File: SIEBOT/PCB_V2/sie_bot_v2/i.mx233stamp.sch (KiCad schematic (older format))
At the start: 0 parts

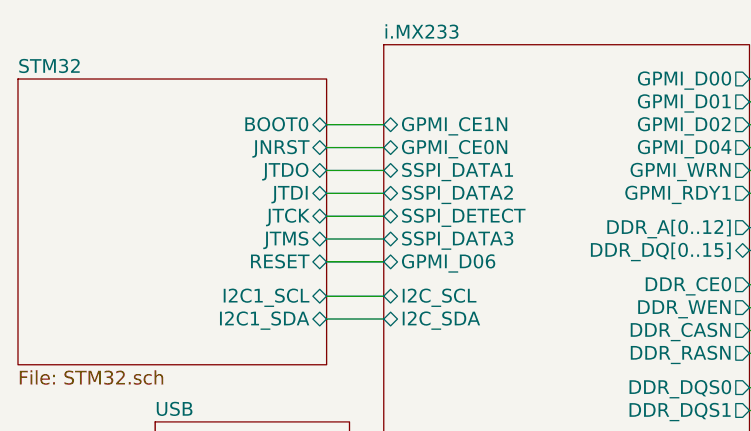
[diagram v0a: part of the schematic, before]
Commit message: Adición de ejemplos, modificación de los fuentes de elua para soportar el stm32f105
Cambios en el PCB para tener comunicación entre el IMX y el STM32 por puerto serial e i2c
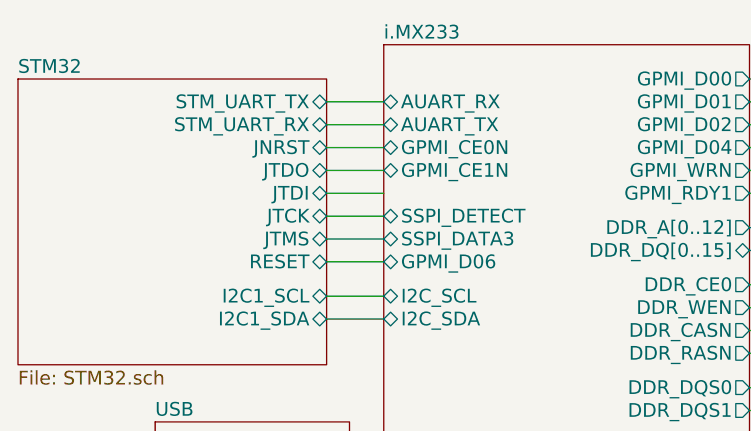
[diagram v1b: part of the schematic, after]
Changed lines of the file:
@@
-EESchema Schematic File Version 2  date Sat 21 Jan 2012 09:46:46 PM COT
+EESchema Schematic File Version 2  date Fri 10 Feb 2012 10:54:05 AM COT
 LIBS:con-jack
 LIBS:adm3101e
@@
 Sheet 1 5
 Title ""
-Date "22 jan 2012"
+Date "10 feb 2012"
 Rev ""
 Comp ""
@@
 $EndDescr
 Wire Wire Line
+	2900 1950 3150 1950
+Wire Wire Line
 	3150 2800 2900 2800
 Wire Wire Line
@@
 	3000 3950 3150 3950
 Wire Wire Line
-	2900 1950 3150 1950
-Wire Wire Line
 	2900 2150 3150 2150
 Wire Wire Line
@@
 Wire Wire Line
 	2900 2700 3150 2700
-$Sheet
-S 1550 1750 1350 1250
-U 4E78AF25
-F0 "STM32" 60
-F1 "STM32.sch" 60
-F2 "BOOT0" B R 2900 1950 60
-F3 "JNRST" B R 2900 2050 60
-F4 "JTMS" B R 2900 2450 60
-F5 "JTCK" B R 2900 2350 60
-F6 "JTDO" B R 2900 2150 60
-F7 "JTDI" B R 2900 2250 60
-F8 "RESET" B R 2900 2550 60
-F9 "I2C1_SCL" B R 2900 2700 60
-F10 "I2C1_SDA" B R 2900 2800 60
-$EndSheet
+Wire Wire Line
+	2900 1850 3150 1850
 $Sheet
 S 3150 1600 1600 2950
@@
 F30 "I2C_SDA" B L 3150 2800 60
 F31 "GPMI_CE0N" B L 3150 2050 60
-F32 "SSPI_DATA1" B L 3150 2150 60
-F33 "SSPI_DETECT" B L 3150 2350 60
-F34 "SSPI_DATA2" B L 3150 2250 60
-F35 "GPMI_CE1N" B L 3150 1950 60
-F36 "GPMI_D06" B L 3150 2550 60
-F37 "SSPI_DATA3" B L 3150 2450 60
-F38 "USM_P2" B L 3150 4150 60
-F39 "USB_M2" B L 3150 4250 60
+F32 "SSPI_DETECT" B L 3150 2350 60
+F33 "GPMI_CE1N" B L 3150 2150 60
+F34 "GPMI_D06" B L 3150 2550 60
+F35 "SSPI_DATA3" B L 3150 2450 60
+F36 "USM_P2" B L 3150 4150 60
+F37 "USB_M2" B L 3150 4250 60
+F38 "AUART_TX" B L 3150 1950 60
+F39 "AUART_RX" B L 3150 1850 60
 $EndSheet
 $Sheet
+S 1550 1750 1350 1250
+U 4E78AF25
+F0 "STM32" 60
+F1 "STM32.sch" 60
+F2 "JNRST" B R 2900 2050 60
+F3 "JTMS" B R 2900 2450 60
+F4 "JTCK" B R 2900 2350 60
+F5 "JTDO" B R 2900 2150 60
+F6 "JTDI" B R 2900 2250 60
+F7 "RESET" B R 2900 2550 60
+F8 "I2C1_SCL" B R 2900 2700 60
+F9 "I2C1_SDA" B R 2900 2800 60
+F10 "STM_UART_TX" B R 2900 1850 60
+F11 "STM_UART_RX" B R 2900 1950 60
+$EndSheet
+$Sheet

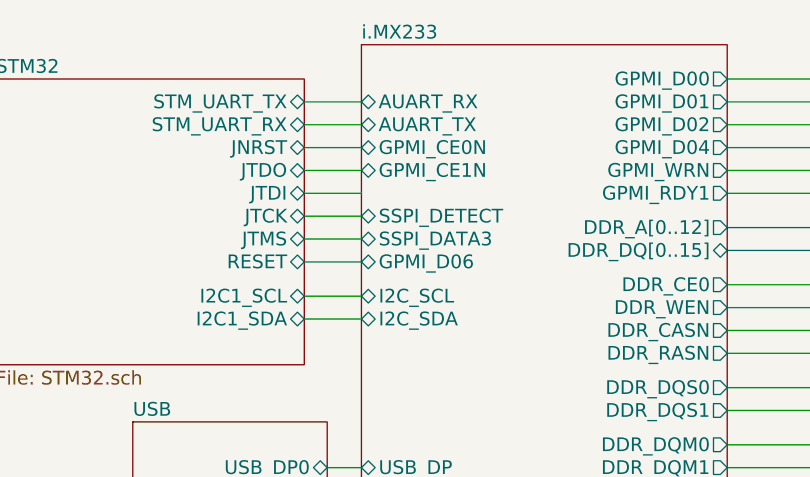
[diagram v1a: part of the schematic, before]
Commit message: Se elimina J2 (jack power) y el pulsador de reset y se dejan estas señales disponibles en los conectores, esto se hace para que esta board se adapte fácil a diferentes plataformas Se cambian las señales TDi y TDO que van del IMX al JTAG del stm32 por PWM2 y GPMI_CE1N, para dejar las señales del I2C del IMX disponibles.
Se conectan las señales SCL (pin 95) y SDA (pin 86) del iMX al bus I2C del STM32.

Se conectan resistencias de pull-up al bus I2C entre el IMX y el STM32

Se coloca una resistencia en serie a la salida de la señal TDO del STM32, esto para evitar que daños cuando los dos chips configuren esta señal como salida.

Se eliminan los conectores individuales de los motores y se organizan en un nuevo conector. Ahora los puentes H tienen el mismo voltaje de alimentación.

Se elimina la conexión entre BOOT0 y el IMX, ya que no es necesario modificar la forma de inicialización. Se elimina la resistencia de pull-up que se conecta a BOOT1.
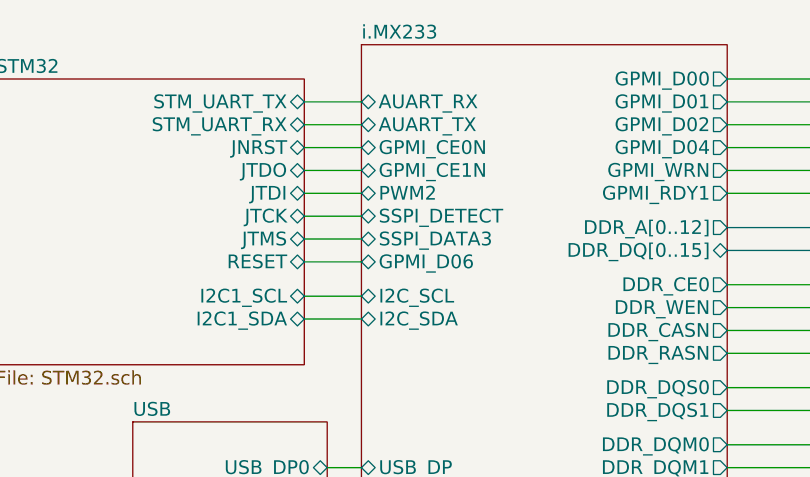
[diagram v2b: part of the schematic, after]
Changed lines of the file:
@@
-EESchema Schematic File Version 2  date Fri 10 Feb 2012 10:54:05 AM COT
+EESchema Schematic File Version 2  date Fri 10 Feb 2012 05:02:18 PM COT
 LIBS:con-jack
 LIBS:adm3101e
@@
 F38 "AUART_TX" B L 3150 1950 60
 F39 "AUART_RX" B L 3150 1850 60
+F40 "PWM2" B L 3150 2250 60
 $EndSheet
 $Sheet

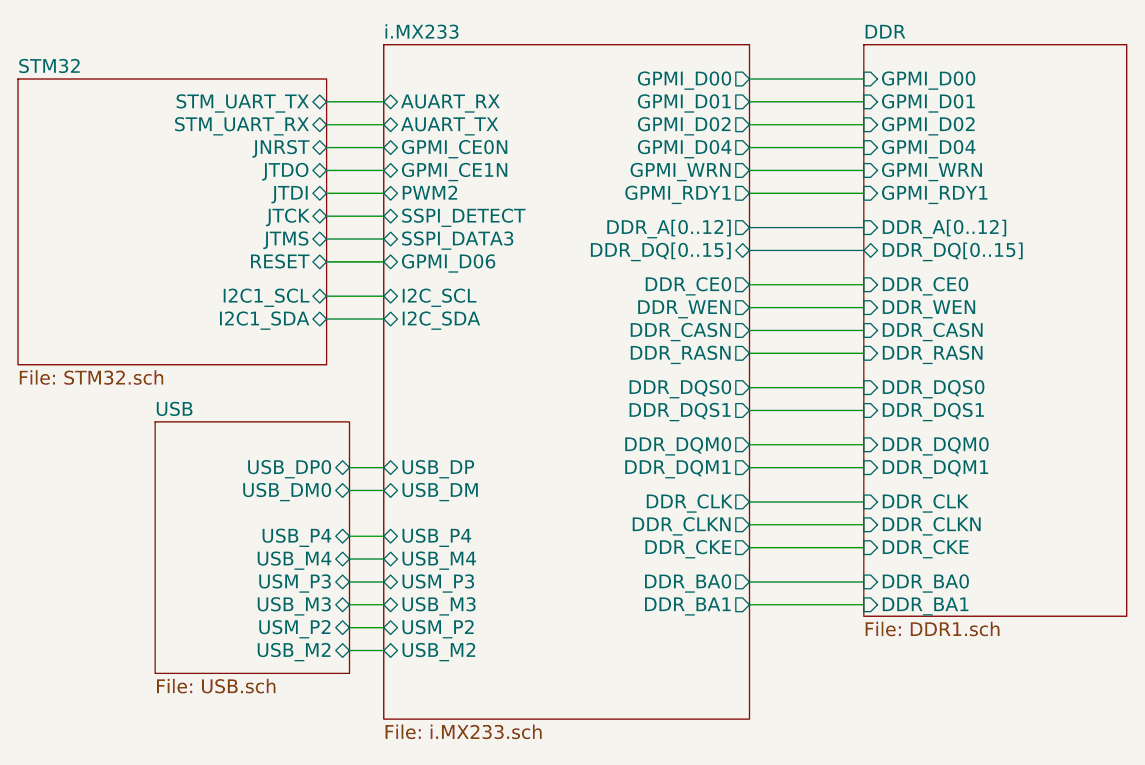
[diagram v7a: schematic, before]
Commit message: Modificacion del reset del hub USB ahora el IMX233 controla el reset
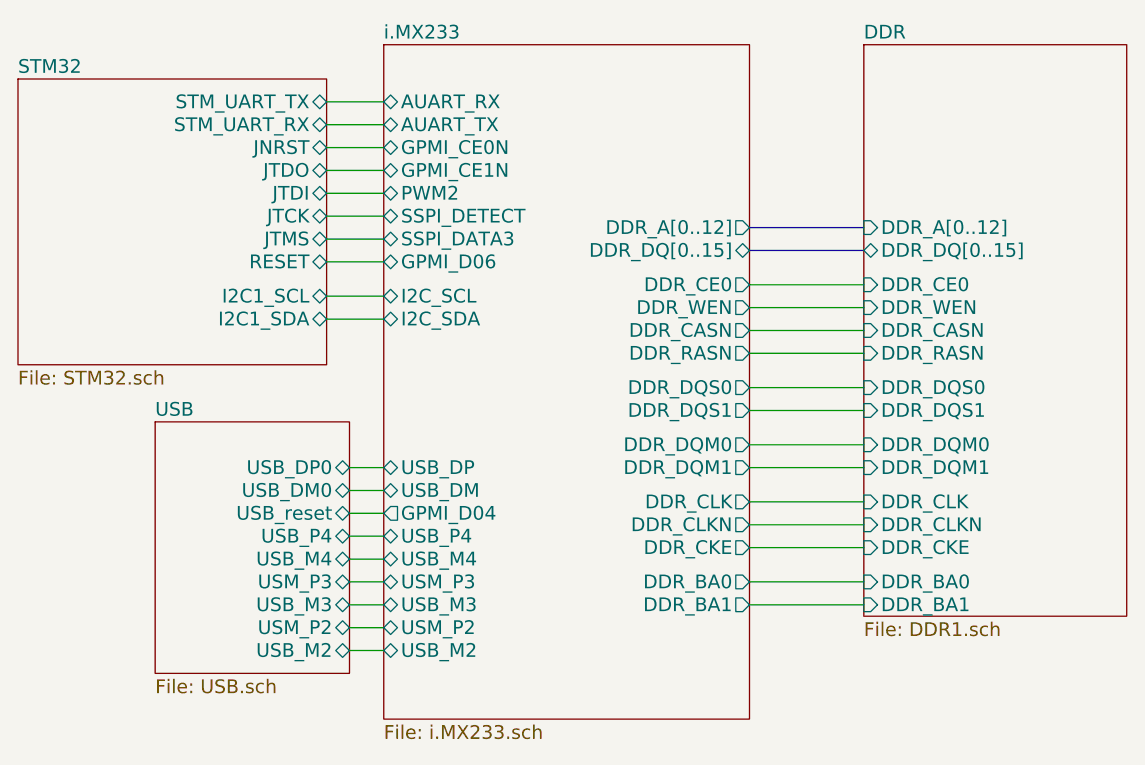
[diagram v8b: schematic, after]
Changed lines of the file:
@@
-EESchema Schematic File Version 2  date Sat 18 Feb 2012 11:36:23 AM COT
+EESchema Schematic File Version 2  date sáb 03 mar 2012 09:20:54 COT
 LIBS:con-jack
 LIBS:adm3101e
@@
 LIBS:zxmhc3f381n8
 LIBS:i.mx233stamp-cache
-EELAYER 25  0
+EELAYER 24  0
 EELAYER END
 $Descr A4 11700 8267
-encoding utf-8
 Sheet 1 5
 Title ""
-Date "18 feb 2012"
+Date "3 mar 2012"
 Rev ""
 Comp ""
@@
 $EndDescr
 Wire Wire Line
-	2900 1950 3150 1950
-Wire Wire Line
-	3150 2800 2900 2800
-Wire Wire Line
-	3000 4250 3150 4250
-Wire Wire Line
-	2900 2550 3150 2550
-Wire Wire Line
-	2900 2250 3150 2250
-Wire Wire Line
-	2900 2050 3150 2050
-Wire Wire Line
-	3000 4050 3150 4050
-Wire Wire Line
-	3000 3850 3150 3850
-Wire Wire Line
-	3000 3550 3150 3550
-Wire Wire Line
-	4750 2250 5250 2250
-Wire Wire Line
-	5250 1950 4750 1950
-Wire Wire Line
-	5250 1750 4750 1750
+	3000 3650 3150 3650
+Wire Wire Line
+	2900 1850 3150 1850
+Wire Wire Line
+	2900 2700 3150 2700
+Wire Wire Line
+	3000 4150 3150 4150
+Wire Wire Line
+	2900 2450 3150 2450
+Wire Wire Line
+	2900 2350 3150 2350
+Wire Wire Line
+	2900 2150 3150 2150
+Wire Wire Line
+	3000 3950 3150 3950
+Wire Wire Line
+	3000 3750 3150 3750
+Wire Wire Line
+	3150 3450 3000 3450
+Wire Bus Line
+	4750 2500 5250 2500
+Wire Wire Line
+	5250 3350 4750 3350
+Wire Wire Line
+	4750 3100 5250 3100
+Wire Wire Line
+	4750 3950 5250 3950
+Wire Wire Line
+	4750 3700 5250 3700
+Wire Wire Line
+	4750 2650 5250 2650
+Wire Wire Line
+	4750 2750 5250 2750
+Wire Wire Line
+	4750 2850 5250 2850
+Wire Wire Line
+	4750 3600 5250 3600
+Wire Wire Line
+	4750 3800 5250 3800
+Wire Wire Line
+	4750 4050 5250 4050
+Wire Wire Line
+	4750 2950 5250 2950
+Wire Wire Line
+	5250 3200 4750 3200
+Wire Wire Line
+	4750 3450 5250 3450
 Wire Bus Line
 	5250 2400 4750 2400
 Wire Wire Line
-	4750 3450 5250 3450
-Wire Wire Line
-	5250 3200 4750 3200
-Wire Wire Line
-	4750 2950 5250 2950
-Wire Wire Line
-	4750 4050 5250 4050
-Wire Wire Line
-	4750 3800 5250 3800
-Wire Wire Line
-	4750 3600 5250 3600
-Wire Wire Line
-	4750 2850 5250 2850
-Wire Wire Line
-	4750 2750 5250 2750
-Wire Wire Line
-	4750 2650 5250 2650
-Wire Wire Line
-	4750 3700 5250 3700
-Wire Wire Line
-	4750 3950 5250 3950
-Wire Wire Line
-	4750 3100 5250 3100
-Wire Wire Line
-	5250 3350 4750 3350
-Wire Wire Line
-	4750 2050 5250 2050
-Wire Bus Line
-	4750 2500 5250 2500
-Wire Wire Line
-	4750 1850 5250 1850
-Wire Wire Line
-	4750 2150 5250 2150
-Wire Wire Line
-	3150 3450 3000 3450
-Wire Wire Line
-	3000 3750 3150 3750
-Wire Wire Line
-	3000 3950 3150 3950
-Wire Wire Line
-	2900 2150 3150 2150
-Wire Wire Line
-	2900 2350 3150 2350
-Wire Wire Line
-	2900 2450 3150 2450
-Wire Wire Line
-	3000 4150 3150 4150
-Wire Wire Line
-	2900 2700 3150 2700
-Wire Wire Line
-	2900 1850 3150 1850
+	3000 3550 3150 3550
+Wire Wire Line
+	3000 3850 3150 3850
+Wire Wire Line
+	3000 4050 3150 4050
+Wire Wire Line
+	2900 2050 3150 2050
+Wire Wire Line
+	2900 2250 3150 2250
+Wire Wire Line
+	2900 2550 3150 2550
+Wire Wire Line
+	3000 4250 3150 4250
+Wire Wire Line
+	3150 2800 2900 2800
+Wire Wire Line
+	2900 1950 3150 1950
 $Sheet
 S 3150 1600 1600 2950
@@
 F15 "DDR_BA1" O R 4750 4050 60
 F16 "DDR_BA0" O R 4750 3950 60
-F17 "GPMI_D04" O R 4750 2050 60
-F18 "GPMI_WRN" O R 4750 2150 60
-F19 "GPMI_RDY1" O R 4750 2250 60
-F20 "GPMI_D00" O R 4750 1750 60
-F21 "GPMI_D01" O R 4750 1850 60
-F22 "GPMI_D02" O R 4750 1950 60
-F23 "USB_DM" B L 3150 3550 60
-F24 "USB_DP" B L 3150 3450 60
-F25 "USB_M3" B L 3150 4050 60
-F26 "USM_P3" B L 3150 3950 60
-F27 "USB_M4" B L 3150 3850 60
-F28 "USB_P4" B L 3150 3750 60
-F29 "I2C_SCL" B L 3150 2700 60
-F30 "I2C_SDA" B L 3150 2800 60
-F31 "GPMI_CE0N" B L 3150 2050 60
-F32 "SSPI_DETECT" B L 3150 2350 60
-F33 "GPMI_CE1N" B L 3150 2150 60
-F34 "GPMI_D06" B L 3150 2550 60
-F35 "SSPI_DATA3" B L 3150 2450 60
-F36 "USM_P2" B L 3150 4150 60
-F37 "USB_M2" B L 3150 4250 60
-F38 "AUART_TX" B L 3150 1950 60
-F39 "AUART_RX" B L 3150 1850 60
-F40 "PWM2" B L 3150 2250 60
-$EndSheet
-$Sheet
-S 1550 1750 1350 1250
-U 4E78AF25
-F0 "STM32" 60
-F1 "STM32.sch" 60
-F2 "JNRST" B R 2900 2050 60
-F3 "JTMS" B R 2900 2450 60
-F4 "JTCK" B R 2900 2350 60
-F5 "JTDO" B R 2900 2150 60
-F6 "JTDI" B R 2900 2250 60
-F7 "RESET" B R 2900 2550 60
-F8 "I2C1_SCL" B R 2900 2700 60
-F9 "I2C1_SDA" B R 2900 2800 60
-F10 "STM_UART_TX" B R 2900 1850 60
-F11 "STM_UART_RX" B R 2900 1950 60
+F17 "USB_DM" B L 3150 3550 60
+F18 "USB_DP" B L 3150 3450 60
+F19 "USB_M3" B L 3150 4050 60
+F20 "USM_P3" B L 3150 3950 60
+F21 "USB_M4" B L 3150 3850 60
+F22 "USB_P4" B L 3150 3750 60
+F23 "I2C_SCL" B L 3150 2700 60
+F24 "I2C_SDA" B L 3150 2800 60
+F25 "GPMI_CE0N" B L 3150 2050 60
+F26 "SSPI_DETECT" B L 3150 2350 60
+F27 "GPMI_CE1N" B L 3150 2150 60
+F28 "GPMI_D06" B L 3150 2550 60
+F29 "SSPI_DATA3" B L 3150 2450 60
+F30 "USM_P2" B L 3150 4150 60
+F31 "USB_M2" B L 3150 4250 60
+F32 "AUART_TX" B L 3150 1950 60
+F33 "AUART_RX" B L 3150 1850 60
+F34 "PWM2" B L 3150 2250 60
+F35 "GPMI_D04" O L 3150 3650 60
 $EndSheet
 $Sheet
@@
 F15 "DDR_RASN" I L 5250 2950 60
 F16 "DDR_WEN" I L 5250 2750 60
-F17 "GPMI_D04" I L 5250 2050 60
-F18 "GPMI_D02" I L 5250 1950 60
-F19 "GPMI_WRN" I L 5250 2150 60
-F20 "GPMI_RDY1" I L 5250 2250 60
-F21 "GPMI_D01" I L 5250 1850 60
-F22 "GPMI_D00" I L 5250 1750 60
+$EndSheet
+$Sheet
+S 1550 1750 1350 1250
+U 4E78AF25
+F0 "STM32" 60
+F1 "STM32.sch" 60
+F2 "JNRST" B R 2900 2050 60
+F3 "JTMS" B R 2900 2450 60
+F4 "JTCK" B R 2900 2350 60
+F5 "JTDO" B R 2900 2150 60
+F6 "JTDI" B R 2900 2250 60
+F7 "RESET" B R 2900 2550 60
+F8 "I2C1_SCL" B R 2900 2700 60
+F9 "I2C1_SDA" B R 2900 2800 60
+F10 "STM_UART_TX" B R 2900 1850 60
+F11 "STM_UART_RX" B R 2900 1950 60
 $EndSheet
 $Sheet
@@
 F8 "USB_M2" B R 3000 4250 60
 F9 "USM_P2" B R 3000 4150 60
+F10 "USB_reset" B R 3000 3650 60
 $EndSheet
 $EndSCHEMATC
